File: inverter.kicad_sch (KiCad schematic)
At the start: 28 parts, among them Q1 IRF530NPBF, Q2 IRF530NPBF, Q3 IRF530NPBF, Q4 IRF530NPBF, U1 IR2110, U2 IR2110

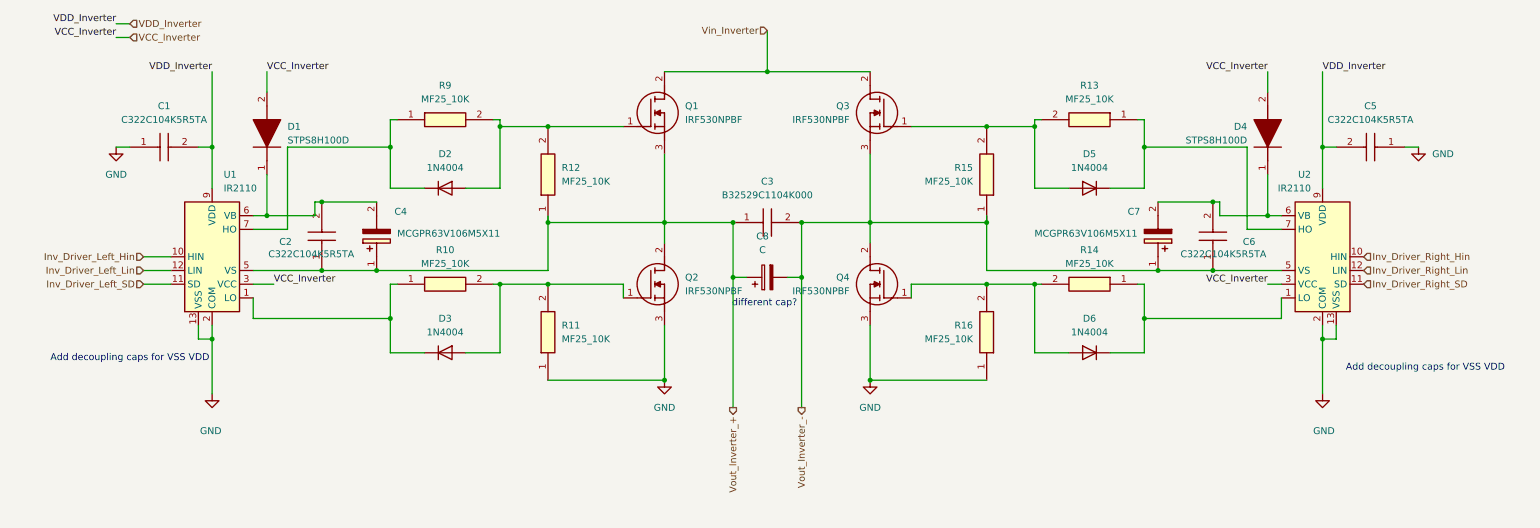
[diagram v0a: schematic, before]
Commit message: SCH Save: 2 files changed inverter.kicad_sch 0/20/0 voltsense_inverter.kicad_sch 232/0/63
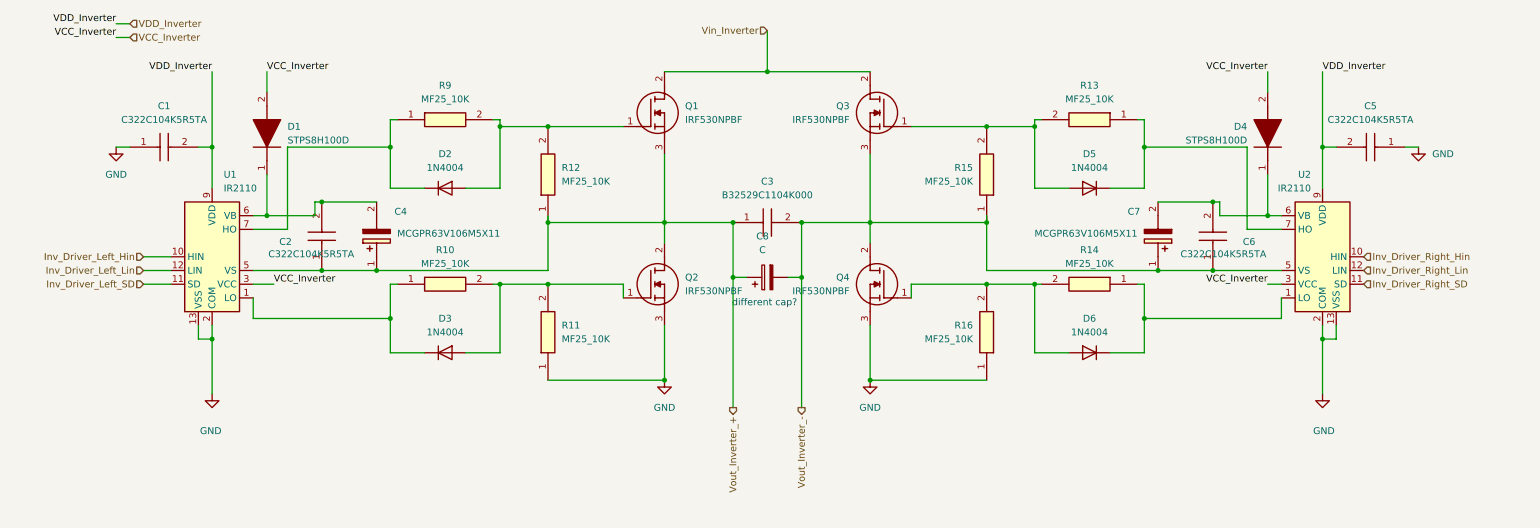
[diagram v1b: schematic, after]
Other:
- note removed: "Add decoupling caps for VSS VDD"
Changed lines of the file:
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@@
 	(generator_version "10.0")
 	(paper "A4")
-	(text "Add decoupling caps for VSS VDD"
-		(exclude_from_sim no)
-		(at 269.24 80.264 0)
-		(effects
-			(font
-				(size 1.27 1.27)
-			)
-		)
-	)
 	(text "different cap?\n"
 		(exclude_from_sim no)
@@
 		(effects
 			(font
-				(size 1.27 1.27)
-			)
-		)
-	)
-	(text "Add decoupling caps for VSS VDD"
-		(exclude_from_sim no)
-		(at 29.21 78.486 0)
-		(effects
-			(font

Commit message: SCH Save: 1 files changed inverter.kicad_sch 20/0/0
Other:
- note added: "Add decoupling caps for VSS VDD"
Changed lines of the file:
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@@
 	(generator_version "10.0")
 	(paper "A4")
+	(text "Add decoupling caps for VSS VDD"
+		(exclude_from_sim no)
+		(at 269.24 80.264 0)
+		(effects
+			(font
+				(size 1.27 1.27)
+			)
+		)
+	)
 	(text "different cap?\n"
 		(exclude_from_sim no)
@@
 		(effects
 			(font
+				(size 1.27 1.27)
+			)
+		)
+	)
+	(text "Add decoupling caps for VSS VDD"
+		(exclude_from_sim no)
+		(at 29.21 78.486 0)
+		(effects
+			(font

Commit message: SCH Save: 1 files changed inverter.kicad_sch 0/0/2
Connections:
- net VCC_Inverter renamed VCC_Driver_Inverter
- net VDD_Inverter renamed VDD_Driver_Inverter
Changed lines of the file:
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@@
 		)
 	)
-	(hierarchical_label "VDD_Inverter"
+	(hierarchical_label "VDD_Driver_Inverter"
 		(shape input)
 		(at 29.21 16.51 0)
@@
 		)
 	)
-	(hierarchical_label "VCC_Inverter"
+	(hierarchical_label "VCC_Driver_Inverter"
 		(shape input)
 		(at 29.21 19.05 0)

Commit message: SCH Save: 2 files changed GateDriver.kicad_sch 0/0/2 inverter.kicad_sch 0/0/2
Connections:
- net VCC_Driver_Inverter renamed VCC_Inverter
- net VDD_Driver_Inverter renamed VDD_Inverter
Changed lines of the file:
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@@
 		)
 	)
-	(hierarchical_label "VDD_Driver_Inverter"
+	(hierarchical_label "VDD_Inverter"
 		(shape input)
 		(at 29.21 16.51 0)
@@
 		)
 	)
-	(hierarchical_label "VCC_Driver_Inverter"
+	(hierarchical_label "VCC_Inverter"
 		(shape input)
 		(at 29.21 19.05 0)

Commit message: Autosave
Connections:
- net VDD_Inverter renamed VDD_Driver_Inverter
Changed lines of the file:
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@@
 		)
 	)
-	(hierarchical_label "VDD_Inverter"
+	(hierarchical_label "VDD_Driver_Inverter"
 		(shape input)
 		(at 29.21 16.51 0)

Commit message: Autosave
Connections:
- net VCC_Inverter renamed VCC_Driver_Inverter
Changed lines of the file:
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@@
 		)
 	)
-	(hierarchical_label "VCC_Inverter"
+	(hierarchical_label "VCC_Driver_Inverter"
 		(shape input)
 		(at 29.21 19.05 0)

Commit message: SCH Save: 1 files changed inverter.kicad_sch 0/0/15
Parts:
- C3: footprint (none) -> Capacitor_THT:C_Rect_L7.0mm_W2.5mm_P5.00mm
- D1, D4: footprint (none) -> Package_TO_SOT_THT:TO-220-2_Vertical
- Q1, Q2, Q3, Q4: footprint (none) -> Package_TO_SOT_THT:TO-220-3_Vertical
- R10, R11, R12, R13, R14, R15, R16, R9: footprint (none) -> Resistor_THT:R_Axial_DIN0207_L6.3mm_D2.5mm_P7.62mm_Horizontal
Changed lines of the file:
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@@
 			)
 		)
-		(property "Footprint" ""
+		(property "Footprint" "Package_TO_SOT_THT:TO-220-3_Vertical"
 			(at 132.08 166.04 0)
 			(hide yes)
@@
 			)
 		)
-		(property "Footprint" ""
+		(property "Footprint" "Resistor_THT:R_Axial_DIN0207_L6.3mm_D2.5mm_P7.62mm_Horizontal"
 			(at 201.93 160.96 0)
 			(hide yes)
@@
 			)
 		)
-		(property "Footprint" ""
+		(property "Footprint" "Package_TO_SOT_THT:TO-220-3_Vertical"
 			(at 162.56 166.04 0)
 			(hide yes)
@@
 			)
 		)
-		(property "Footprint" ""
+		(property "Footprint" "Resistor_THT:R_Axial_DIN0207_L6.3mm_D2.5mm_P7.62mm_Horizontal"
 			(at 91.77 68.58 0)
 			(hide yes)
@@
 			)
 		)
-		(property "Footprint" ""
+		(property "Footprint" "Package_TO_SOT_THT:TO-220-3_Vertical"
 			(at 132.08 134.29 0)
 			(hide yes)
@@
 			)
 		)
-		(property "Footprint" ""
+		(property "Footprint" "Resistor_THT:R_Axial_DIN0207_L6.3mm_D2.5mm_P7.62mm_Horizontal"
 			(at 202.87 39.37 0)
 			(hide yes)
@@
 			)
 		)
-		(property "Footprint" ""
+		(property "Footprint" "Resistor_THT:R_Axial_DIN0207_L6.3mm_D2.5mm_P7.62mm_Horizontal"
 			(at 92.71 160.96 0)
 			(hide yes)
@@
 			)
 		)
-		(property "Footprint" ""
+		(property "Footprint" "Resistor_THT:R_Axial_DIN0207_L6.3mm_D2.5mm_P7.62mm_Horizontal"
 			(at 202.87 68.58 0)
 			(hide yes)
@@
 			)
 		)
-		(property "Footprint" ""
+		(property "Footprint" "Package_TO_SOT_THT:TO-220-2_Vertical"
 			(at 142.57 33.02 0)
 			(hide yes)
@@
 			)
 		)
-		(property "Footprint" ""
+		(property "Footprint" "Capacitor_THT:C_Rect_L7.0mm_W2.5mm_P5.00mm"
 			(at 149.86 149.53 0)
 			(hide yes)
@@
 			)
 		)
-		(property "Footprint" ""
+		(property "Footprint" "Resistor_THT:R_Axial_DIN0207_L6.3mm_D2.5mm_P7.62mm_Horizontal"
 			(at 92.71 130.48 0)
 			(hide yes)
@@
 			)
 		)
-		(property "Footprint" ""
+		(property "Footprint" "Resistor_THT:R_Axial_DIN0207_L6.3mm_D2.5mm_P7.62mm_Horizontal"
 			(at 91.77 39.37 0)
 			(hide yes)
@@
 			)
 		)
-		(property "Footprint" ""
+		(property "Footprint" "Resistor_THT:R_Axial_DIN0207_L6.3mm_D2.5mm_P7.62mm_Horizontal"
 			(at 201.93 130.48 0)
 			(hide yes)
@@
 			)
 		)
-		(property "Footprint" ""
+		(property "Footprint" "Package_TO_SOT_THT:TO-220-2_Vertical"
 			(at 152.07 33.02 0)
 			(hide yes)
@@
 			)
 		)
-		(property "Footprint" ""
+		(property "Footprint" "Package_TO_SOT_THT:TO-220-3_Vertical"
 			(at 162.56 134.29 0)
 			(hide yes)

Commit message: SCH Save: 1 files changed inverter.kicad_sch 0/0/6
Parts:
- C1, C2, C5, C6: footprint (none) -> Capacitor_THT:C_Disc_D4.3mm_W1.9mm_P5.00mm
- C4, C7: footprint (none) -> Capacitor_THT:C_Radial_D5.0mm_H11.0mm_P2.00mm
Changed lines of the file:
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@@
 			)
 		)
-		(property "Footprint" ""
+		(property "Footprint" "Capacitor_THT:C_Disc_D4.3mm_W1.9mm_P5.00mm"
 			(at 133.68 53.34 0)
 			(hide yes)
@@
 			)
 		)
-		(property "Footprint" ""
+		(property "Footprint" "Capacitor_THT:C_Radial_D5.0mm_H11.0mm_P2.00mm"
 			(at 123.52 53.34 0)
 			(hide yes)
@@
 			)
 		)
-		(property "Footprint" ""
+		(property "Footprint" "Capacitor_THT:C_Disc_D4.3mm_W1.9mm_P5.00mm"
 			(at 256.54 135.56 0)
 			(hide yes)
@@
 			)
 		)
-		(property "Footprint" ""
+		(property "Footprint" "Capacitor_THT:C_Disc_D4.3mm_W1.9mm_P5.00mm"
 			(at 38.1 135.56 0)
 			(hide yes)
@@
 			)
 		)
-		(property "Footprint" ""
+		(property "Footprint" "Capacitor_THT:C_Disc_D4.3mm_W1.9mm_P5.00mm"
 			(at 160.96 53.34 0)
 			(hide yes)
@@
 			)
 		)
-		(property "Footprint" ""
+		(property "Footprint" "Capacitor_THT:C_Radial_D5.0mm_H11.0mm_P2.00mm"
 			(at 171.12 53.34 0)
 			(hide yes)
